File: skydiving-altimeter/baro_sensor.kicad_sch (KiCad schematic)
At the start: 3 parts, among them U2 BMP581

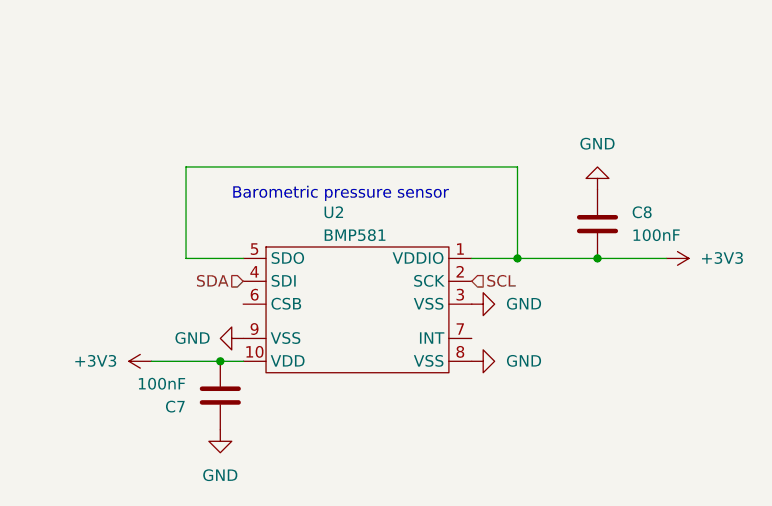
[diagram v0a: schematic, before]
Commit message: Began adding 10 ohm current limiting resistors
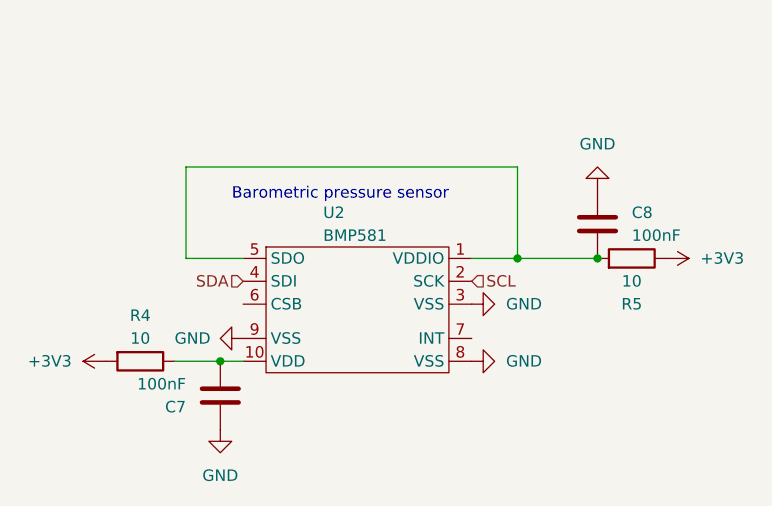
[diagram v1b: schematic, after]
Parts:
- added R4, R5: 10, Resistor_SMD:R_0402_1005Metric, symbol Device:R
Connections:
- net +3V3: now also R4.2, R5.1; no longer C7.2, C8.2, U2.1 (VDDIO), U2.10 (VDD), U2.5 (SDO)
- new net: C7.2, R4.1, U2.10 (VDD)
- new net: C8.2, R5.2, U2.1 (VDDIO), U2.5 (SDO)

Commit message: Fixed CSB pin routing
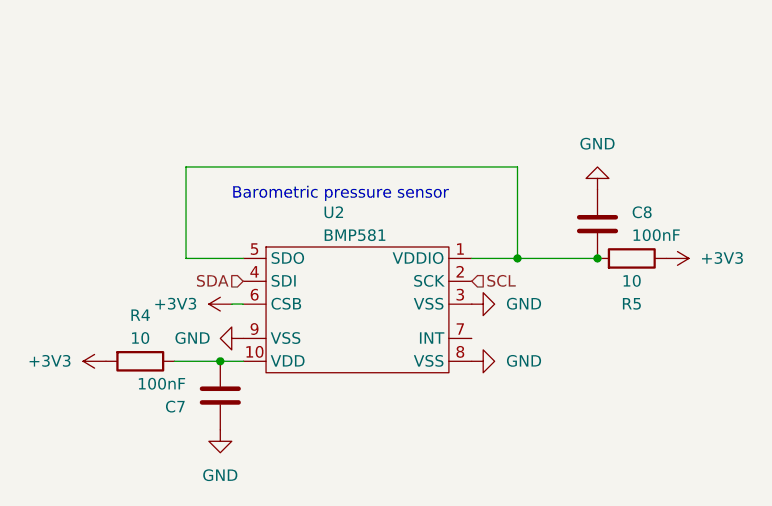
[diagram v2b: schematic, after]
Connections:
- net +3V3: now also U2.6 (CSB)
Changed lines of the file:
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@@
+    (stroke (width 0) (type default))
+  )
+  (wire (pts (xy 120.65 90.17) (xy 121.92 90.17))
     (stroke (width 0) (type default))
   )
@@
         )
       )
+    )
+  )
+  (symbol (lib_id "power:+3V3") (at 120.65 90.17 90) (mirror x) (unit 1)
+    (in_bom yes) (on_board yes) (dnp no)
+    (property "Reference" "#PWR02" (at 124.46 90.17 0)
+      (effects (font (size 1.27 1.27)) hide)
+    )
+    (property "Value" "+3V3" (at 116.84 90.1699 90)
+      (effects (font (size 1.27 1.27)) (justify left))
+    )
+    (property "Footprint" "" (at 120.65 90.17 0)
+      (effects (font (size 1.27 1.27)) hide)
+    )
+    (property "Datasheet" "" (at 120.65 90.17 0)
+      (effects (font (size 1.27 1.27)) hide)
+    )
+    (pin "1")
+    (instances
+      (project "skydiving-altimeter"
+        (path "/e63e39d7-6ac0-4ffd-8aa3-1841a4541b55/25087f50-b4bd-4ba8-9294-4cb0f29516ca"
+          (reference "#PWR02") (unit 1)
+        )
+      )

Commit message: Switched most components to 0402
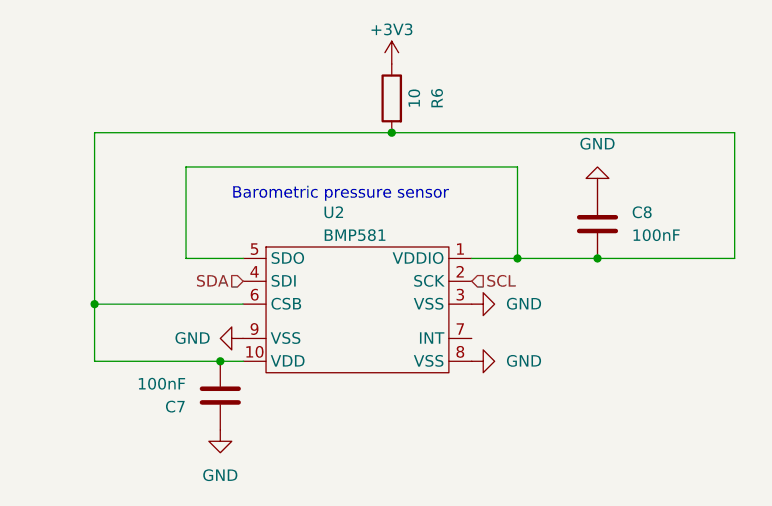
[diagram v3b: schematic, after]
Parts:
- removed R4, R5: 10, Resistor_SMD:R_0402_1005Metric, symbol Device:R
- added R6: 10, Resistor_SMD:R_0402_1005Metric, symbol Device:R
- C7, C8: footprint Capacitor_SMD:C_0805_2012Metric -> Capacitor_SMD:C_0402_1005Metric
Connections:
- net +3V3: now also R6.1; no longer U2.6 (CSB)
- net at C7.2, U2.10 (VDD): now also C8.2, U2.1 (VDDIO), U2.5 (SDO), U2.6 (CSB), R6.2
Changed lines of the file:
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@@
 (kicad_sch (version 20230121) (generator eeschema)
   (paper "A4")
+  (junction (at 138.43 71.12) (diameter 0) (color 0 0 0 0)
+  )
+  (junction (at 119.38 96.52) (diameter 0) (color 0 0 0 0)
+  )
+  (junction (at 152.4 85.09) (diameter 0) (color 0 0 0 0)
+  )
   (junction (at 161.29 85.09) (diameter 0) (color 0 0 0 0)
   )
-  (junction (at 119.38 96.52) (diameter 0) (color 0 0 0 0)
-  )
-  (junction (at 152.4 85.09) (diameter 0) (color 0 0 0 0)
+  (junction (at 105.41 90.17) (diameter 0) (color 0 0 0 0)
   )
   (wire (pts (xy 121.92 96.52) (xy 119.38 96.52))
@@
     (stroke (width 0) (type default))
   )
-  (wire (pts (xy 114.3 96.52) (xy 119.38 96.52))
-    (stroke (width 0) (type default))
-  )
-  (wire (pts (xy 120.65 90.17) (xy 121.92 90.17))
+  (wire (pts (xy 176.53 85.09) (xy 161.29 85.09))
+    (stroke (width 0) (type default))
+  )
+  (wire (pts (xy 105.41 96.52) (xy 119.38 96.52))
+    (stroke (width 0) (type default))
+  )
+  (wire (pts (xy 105.41 71.12) (xy 105.41 90.17))
+    (stroke (width 0) (type default))
+  )
+  (wire (pts (xy 138.43 71.12) (xy 105.41 71.12))
+    (stroke (width 0) (type default))
+  )
+  (wire (pts (xy 105.41 90.17) (xy 121.92 90.17))
+    (stroke (width 0) (type default))
+  )
+  (wire (pts (xy 138.43 71.12) (xy 176.53 71.12))
+    (stroke (width 0) (type default))
+  )
+  (wire (pts (xy 105.41 90.17) (xy 105.41 96.52))
+    (stroke (width 0) (type default))
+  )
+  (wire (pts (xy 176.53 71.12) (xy 176.53 85.09))
     (stroke (width 0) (type default))
   )
@@
     (effects (font (size 1.27 1.27)) (justify right))
   )
-  (symbol (lib_id "Device:R") (at 110.49 96.52 270) (unit 1)
-    (in_bom yes) (on_board yes) (dnp no) (fields_autoplaced)
-    (property "Reference" "R4" (at 110.49 91.44 90)
-      (effects (font (size 1.27 1.27)))
-    )
-    (property "Value" "10" (at 110.49 93.98 90)
-      (effects (font (size 1.27 1.27)))
-    )
-    (property "Footprint" "Resistor_SMD:R_0402_1005Metric" (at 110.49 94.742 90)
-      (effects (font (size 1.27 1.27)) hide)
-    )
-    (property "Datasheet" "~" (at 110.49 96.52 0)
+  (symbol (lib_id "Device:C") (at 161.29 81.28 0) (unit 1)
+    (in_bom yes) (on_board yes) (dnp no) (fields_autoplaced)
+    (property "Reference" "C8" (at 165.1 80.0099 0)
+      (effects (font (size 1.27 1.27)) (justify left))
+    )
+    (property "Value" "100nF" (at 165.1 82.5499 0)
+      (effects (font (size 1.27 1.27)) (justify left))
+    )
+    (property "Footprint" "Capacitor_SMD:C_0402_1005Metric" (at 162.2552 85.09 0)
+      (effects (font (size 1.27 1.27)) hide)
+    )
+    (property "Datasheet" "~" (at 161.29 81.28 0)
       (effects (font (size 1.27 1.27)) hide)
     )
@@
       (project "skydiving-altimeter"
         (path "/e63e39d7-6ac0-4ffd-8aa3-1841a4541b55/25087f50-b4bd-4ba8-9294-4cb0f29516ca"
-          (reference "R4") (unit 1)
-        )
-      )
-    )
-  )
-  (symbol (lib_id "Device:C") (at 161.29 81.28 0) (unit 1)
-    (in_bom yes) (on_board yes) (dnp no) (fields_autoplaced)
-    (property "Reference" "C8" (at 165.1 80.0099 0)
-      (effects (font (size 1.27 1.27)) (justify left))
-    )
-    (property "Value" "100nF" (at 165.1 82.5499 0)
-      (effects (font (size 1.27 1.27)) (justify left))
-    )
-    (property "Footprint" "Capacitor_SMD:C_0805_2012Metric" (at 162.2552 85.09 0)
-      (effects (font (size 1.27 1.27)) hide)
-    )
-    (property "Datasheet" "~" (at 161.29 81.28 0)
-      (effects (font (size 1.27 1.27)) hide)
-    )
-    (pin "1")
-    (pin "2")
-    (instances
-      (project "skydiving-altimeter"
-        (path "/e63e39d7-6ac0-4ffd-8aa3-1841a4541b55/25087f50-b4bd-4ba8-9294-4cb0f29516ca"
           (reference "C8") (unit 1)
         )
@@
     )
   )
-  (symbol (lib_id "power:+3V3") (at 120.65 90.17 90) (mirror x) (unit 1)
-    (in_bom yes) (on_board yes) (dnp no)
-    (property "Reference" "#PWR02" (at 124.46 90.17 0)
-      (effects (font (size 1.27 1.27)) hide)
-    )
-    (property "Value" "+3V3" (at 116.84 90.1699 90)
-      (effects (font (size 1.27 1.27)) (justify left))
-    )
-    (property "Footprint" "" (at 120.65 90.17 0)
-      (effects (font (size 1.27 1.27)) hide)
-    )
-    (property "Datasheet" "" (at 120.65 90.17 0)
-      (effects (font (size 1.27 1.27)) hide)
-    )
-    (pin "1")
-    (instances
-      (project "skydiving-altimeter"
-        (path "/e63e39d7-6ac0-4ffd-8aa3-1841a4541b55/25087f50-b4bd-4ba8-9294-4cb0f29516ca"
-          (reference "#PWR02") (unit 1)
-        )
-      )
-    )
-  )
   (symbol (lib_id "power:GND") (at 119.38 104.14 0) (mirror y) (unit 1)
     (in_bom yes) (on_board yes) (dnp no) (fields_autoplaced)
@@
       (effects (font (size 1.27 1.27)) (justify left))
     )
-    (property "Footprint" "Capacitor_SMD:C_0805_2012Metric" (at 118.4148 96.52 0)
+    (property "Footprint" "Capacitor_SMD:C_0402_1005Metric" (at 118.4148 96.52 0)
       (effects (font (size 1.27 1.27)) hide)
     )
@@
     )
   )
-  (symbol (lib_id "power:+3V3") (at 168.91 85.09 270) (unit 1)
-    (in_bom yes) (on_board yes) (dnp no) (fields_autoplaced)
-    (property "Reference" "#PWR0118" (at 165.1 85.09 0)
-      (effects (font (size 1.27 1.27)) hide)
-    )
-    (property "Value" "+3V3" (at 172.72 85.0899 90)
-      (effects (font (size 1.27 1.27)) (justify left))
-    )
-    (property "Footprint" "" (at 168.91 85.09 0)
-      (effects (font (size 1.27 1.27)) hide)
-    )
-    (property "Datasheet" "" (at 168.91 85.09 0)
-      (effects (font (size 1.27 1.27)) hide)
-    )
-    (pin "1")
-    (instances
-      (project "skydiving-altimeter"
-        (path "/e63e39d7-6ac0-4ffd-8aa3-1841a4541b55/25087f50-b4bd-4ba8-9294-4cb0f29516ca"
-          (reference "#PWR0118") (unit 1)
-        )
-      )
-    )
-  )
   (symbol (lib_id "power:GND") (at 161.29 77.47 0) (mirror x) (unit 1)
     (in_bom yes) (on_board yes) (dnp no) (fields_autoplaced)
@@
     )
   )
-  (symbol (lib_id "power:+3V3") (at 106.68 96.52 90) (unit 1)
-    (in_bom yes) (on_board yes) (dnp no) (fields_autoplaced)
-    (property "Reference" "#PWR0115" (at 110.49 96.52 0)
-      (effects (font (size 1.27 1.27)) hide)
-    )
-    (property "Value" "+3V3" (at 102.87 96.5201 90)
-      (effects (font (size 1.27 1.27)) (justify left))
-    )
-    (property "Footprint" "" (at 106.68 96.52 0)
-      (effects (font (size 1.27 1.27)) hide)
-    )
-    (property "Datasheet" "" (at 106.68 96.52 0)
-      (effects (font (size 1.27 1.27)) hide)
-    )
-    (pin "1")
-    (instances
-      (project "skydiving-altimeter"
-        (path "/e63e39d7-6ac0-4ffd-8aa3-1841a4541b55/25087f50-b4bd-4ba8-9294-4cb0f29516ca"
-          (reference "#PWR0115") (unit 1)
-        )
-      )
-    )
-  )
-  (symbol (lib_id "Device:R") (at 165.1 85.09 270) (mirror x) (unit 1)
+  (symbol (lib_id "power:+3V3") (at 138.43 63.5 0) (unit 1)
+    (in_bom yes) (on_board yes) (dnp no) (fields_autoplaced)
+    (property "Reference" "#PWR03" (at 138.43 67.31 0)
+      (effects (font (size 1.27 1.27)) hide)
+    )
+    (property "Value" "+3V3" (at 138.43 59.69 0)
+      (effects (font (size 1.27 1.27)))
+    )
+    (property "Footprint" "" (at 138.43 63.5 0)
+      (effects (font (size 1.27 1.27)) hide)
+    )
+    (property "Datasheet" "" (at 138.43 63.5 0)
+      (effects (font (size 1.27 1.27)) hide)
+    )
+    (pin "1")
+    (instances
+      (project "skydiving-altimeter"
+        (path "/e63e39d7-6ac0-4ffd-8aa3-1841a4541b55/25087f50-b4bd-4ba8-9294-4cb0f29516ca"
+          (reference "#PWR03") (unit 1)
+        )
+      )
+    )
+  )
+  (symbol (lib_id "Device:R") (at 138.43 67.31 0) (mirror y) (unit 1)
     (in_bom yes) (on_board yes) (dnp no)
-    (property "Reference" "R5" (at 165.1 90.17 90)
-      (effects (font (size 1.27 1.27)))
-    )
-    (property "Value" "10" (at 165.1 87.63 90)
-      (effects (font (size 1.27 1.27)))
-    )
-    (property "Footprint" "Resistor_SMD:R_0402_1005Metric" (at 165.1 86.868 90)
-      (effects (font (size 1.27 1.27)) hide)
-    )
-    (property "Datasheet" "~" (at 165.1 85.09 0)
+    (property "Reference" "R6" (at 143.51 67.31 90)
+      (effects (font (size 1.27 1.27)))
+    )
+    (property "Value" "10" (at 140.97 67.31 90)
+      (effects (font (size 1.27 1.27)))
+    )
+    (property "Footprint" "Resistor_SMD:R_0402_1005Metric" (at 140.208 67.31 90)
+      (effects (font (size 1.27 1.27)) hide)
+    )
+    (property "Datasheet" "~" (at 138.43 67.31 0)
       (effects (font (size 1.27 1.27)) hide)
     )
@@
       (project "skydiving-altimeter"
         (path "/e63e39d7-6ac0-4ffd-8aa3-1841a4541b55/25087f50-b4bd-4ba8-9294-4cb0f29516ca"
-          (reference "R5") (unit 1)
-        )
-      )
+          (reference "R6") (unit 1)
+        )
+      )
